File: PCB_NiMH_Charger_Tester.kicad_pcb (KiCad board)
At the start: 2 copper layers, 94.9 x 77.5 mm, 63 parts, among them J1 USB_C_Receptacle_PowerOnly_6P, J2 USB_C_Receptacle_USB2.0_16P, J3 UPDI header, J4 SSD1306, J5 Serial Header, Q1 DTC114EL, Q2 DTA114EL, Q3 MTB060P06I3, Q4 MTA100N10KRI3, SW1 SW_Push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

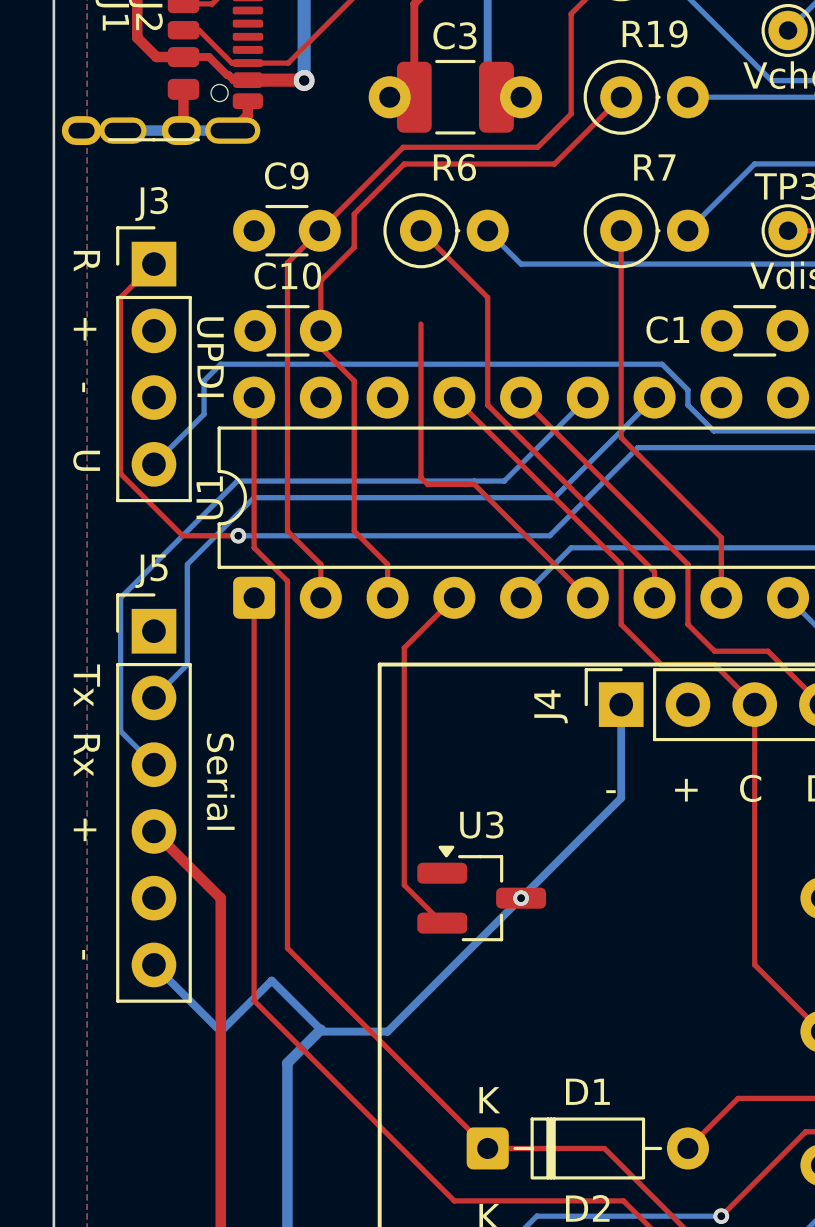
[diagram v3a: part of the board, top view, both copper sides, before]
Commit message: Adjust J3,J5 position
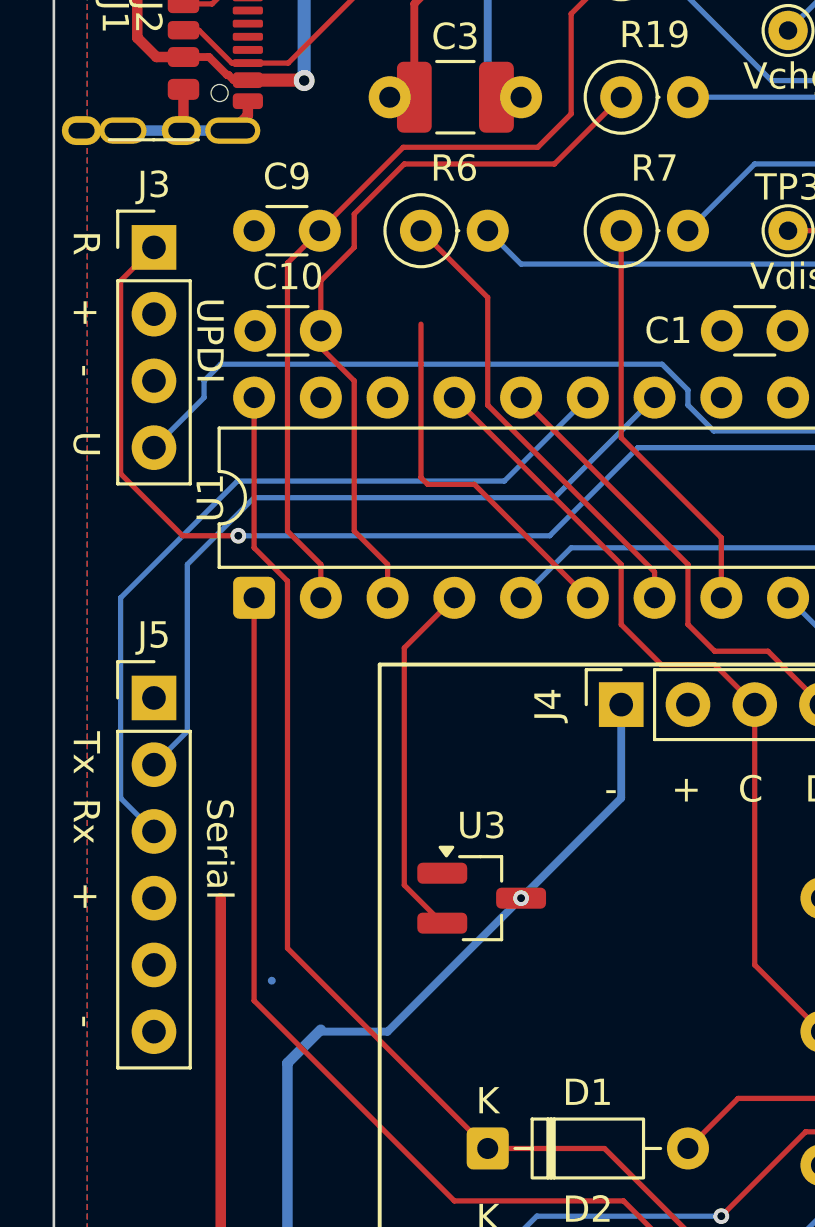
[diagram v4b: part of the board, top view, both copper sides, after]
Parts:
- moved J5 2.54 mm to (53.3, 64.8)
- moved J3 0.63 mm to (53.3, 47.6)
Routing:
- net GND: track 161.9 -> 153.0 mm
- net +5V: track 204.2 -> 200.6 mm
- net TX: track 26.0 -> 28.6 mm
- net RX: track 27.8 -> 30.4 mm
- net UPDI: track 30.9 -> 30.3 mm
- net RESET: track 42.1 -> 42.8 mm
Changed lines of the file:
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@@
 	(footprint "Connector_PinHeader_2.54mm:PinHeader_1x04_P2.54mm_Vertical"
 		(layer "F.Cu")
-		(at 53.34 48.26)
+		(at 53.34 47.625)
 		(descr "Through hole straight pin header, 1x04, 2.54mm pitch, single row")
 		(tags "Through hole pin header THT 1x04 2.54mm single row")
@@
 	(footprint "Connector_PinHeader_2.54mm:PinHeader_1x06_P2.54mm_Vertical"
 		(layer "F.Cu")
-		(at 53.34 62.23)
+		(at 53.34 64.77)
 		(descr "Through hole straight pin header, 1x06, 2.54mm pitch, single row")
 		(tags "Through hole pin header THT 1x06 2.54mm single row")
@@
 	)
 	(gr_text "U"
-		(at 50.165 55.245 270)
+		(at 50.165 54.61 270)
 		(layer "F.SilkS")
 		(effects
@@
 	)
 	(gr_text "UPDI"
-		(at 54.87157 50.165 270)
+		(at 54.87157 49.53 270)
 		(layer "F.SilkS")
 		(effects
@@
 	)
 	(gr_text "Rx"
-		(at 50.165 66.04 270)
+		(at 50.165 68.58 270)
 		(layer "F.SilkS")
 		(effects
@@
 	)
 	(gr_text "Serial"
-		(at 55.245 66.04 270)
+		(at 55.245 68.58 270)
 		(layer "F.SilkS")
 		(effects
@@
 	)
 	(gr_text "R"
-		(at 50.165 47.625 270)
+		(at 50.165 46.99 270)
 		(layer "F.SilkS")
 		(effects
@@
 	)
 	(gr_text "+"
-		(at 50.165 69.215 270)
+		(at 50.165 71.755 270)
 		(layer "F.SilkS")
 		(effects
@@
 	)
 	(gr_text "-"
-		(at 50.165 52.705 270)
+		(at 50.165 52.07 270)
 		(layer "F.SilkS")
 		(effects
@@
 	)
 	(gr_text "Tx"
-		(at 50.165 63.5 270)
+		(at 50.165 66.04 270)
 		(layer "F.SilkS")
 		(effects
@@
 	)
 	(gr_text "-"
-		(at 50.165 74.295 270)
+		(at 50.165 76.835 270)
 		(layer "F.SilkS")
 		(effects
@@
 	)
 	(gr_text "+"
-		(at 50.165 50.165 270)
+		(at 50.165 49.53 270)
 		(layer "F.SilkS")
 		(effects
@@
 	)
 	(segment
-		(start 55.88 77.47)
-		(end 57.82 75.53)
-		(width 0.3)
-		(layer "B.Cu")
-		(net 2)
-	)
-	(segment
 		(start 66.04 35.56)
 		(end 67.31 36.83)
@@
 	)
 	(segment
-		(start 57.825 75.53)
-		(end 59.69 77.395)
-		(width 0.3)
-		(layer "B.Cu")
-		(net 2)
-	)
-	(segment
 		(start 58.42 78.665)
 		(end 59.69 77.395)
@@
 	)
 	(segment
-		(start 53.34 74.93)
-		(end 55.88 77.47)
-		(width 0.3)
-		(layer "B.Cu")
-		(net 2)
-	)
-	(segment
 		(start 116.84 88.9)
 		(end 116.76 88.9)
@@
 	)
 	(segment
-		(start 55.88 72.39)
-		(end 53.34 69.85)
-		(width 0.4)
-		(layer "F.Cu")
-		(net 4)
-	)
-	(segment
 		(start 134.62 96.52)
 		(end 135.89 96.52)
@@
 	)
 	(segment
-		(start 55.245 53.975)
-		(end 53.34 55.88)
+		(start 55.245 53.34)
+		(end 55.245 52.705)
 		(width 0.2)
 		(layer "B.Cu")
@@
 	)
 	(segment
-		(start 78.74 54.61)
-		(end 74.64295 54.61)
+		(start 53.34 55.245)
+		(end 55.245 53.34)
 		(width 0.2)
 		(layer "B.Cu")
@@
 	)
 	(segment
-		(start 55.245 52.705)
-		(end 55.245 53.975)
+		(start 78.74 54.61)
+		(end 74.64295 54.61)
 		(width 0.2)
 		(layer "B.Cu")
@@
 	)
 	(segment
-		(start 54.61 59.69)
-		(end 54.61 63.5)
+		(start 68.58 57.15)
+		(end 72.39 53.34)
 		(width 0.2)
 		(layer "B.Cu")
@@
 	)
 	(segment
-		(start 54.61 63.5)
-		(end 53.34 64.77)
+		(start 53.34 67.31)
+		(end 54.61 66.04)
 		(width 0.2)
 		(layer "B.Cu")
@@
 	)
 	(segment
-		(start 68.58 57.15)
-		(end 57.15 57.15)
+		(start 54.61 66.04)
+		(end 54.61 59.69)
 		(width 0.2)
 		(layer "B.Cu")
@@
 	)
 	(segment
-		(start 57.15 57.15)
-		(end 54.61 59.69)
+		(start 54.61 59.69)
+		(end 57.15 57.15)
 		(width 0.2)
 		(layer "B.Cu")
@@
 	)
 	(segment
-		(start 72.39 53.34)
+		(start 57.15 57.15)
 		(end 68.58 57.15)
 		(width 0.2)
@@
 	)
 	(segment
-		(start 53.34 67.31)
-		(end 52.07 66.04)
-		(width 0.2)
-		(layer "B.Cu")
-		(net 27)
-	)
-	(segment
-		(start 52.07 60.96)
-		(end 56.515 56.515)
+		(start 66.675 56.515)
+		(end 69.85 53.34)
 		(width 0.2)
 		(layer "B.Cu")
@@
 	(segment
 		(start 56.515 56.515)
-		(end 65.532 56.515)
+		(end 66.675 56.515)
 		(width 0.2)
 		(layer "B.Cu")
@@
 	)
 	(segment
-		(start 66.675 56.515)
-		(end 65.532 56.515)
+		(start 53.34 69.85)
+		(end 52.07 68.58)
 		(width 0.2)
 		(layer "B.Cu")
@@
 	)
 	(segment
-		(start 69.85 53.34)
-		(end 66.675 56.515)
+		(start 52.07 68.58)
+		(end 52.07 60.96)
 		(width 0.2)
 		(layer "B.Cu")
@@
 	)
 	(segment
-		(start 52.07 66.04)
-		(end 52.07 60.96)
+		(start 52.07 60.96)
+		(end 56.515 56.515)
 		(width 0.2)
 		(layer "B.Cu")
@@
 	)
 	(segment
-		(start 52.07 49.53)
-		(end 53.34 48.26)
+		(start 53.34 47.625)
+		(end 52.07 48.895)
 		(width 0.2)
 		(layer "F.Cu")
@@
 	)
 	(segment
-		(start 56.55 58.598527)
+		(start 52.07 56.23776)
 		(end 54.430767 58.598527)
 		(width 0.2)
@@
 	)
 	(segment
-		(start 52.07 56.23776)
-		(end 52.07 49.53)
+		(start 52.07 48.895)
+		(end 52.07 56.23776)
 		(width 0.2)
 		(layer "F.Cu")
@@
 	(segment
 		(start 54.430767 58.598527)
-		(end 52.07 56.23776)
+		(end 56.55 58.598527)
 		(width 0.2)
 		(layer "F.Cu")

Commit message: Adjust resistor values
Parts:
- J3: value UPDI header -> UPDI v2 header
- R10, R11: value 1k -> 4.7k
- R12, R15: value 10k -> 47k
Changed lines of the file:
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@@
 			)
 		)
-		(property "Value" "1k"
+		(property "Value" "4.7k"
 			(at 1.27 2.37 0)
 			(layer "F.Fab")
@@
 			)
 		)
-		(property "Value" "10k"
+		(property "Value" "47k"
 			(at 1.27 2.37 0)
 			(layer "F.Fab")
@@
 			)
 		)
-		(property "Value" "UPDI header"
+		(property "Value" "UPDI v2 header"
 			(at 0 10 0)
 			(layer "F.Fab")
@@
 			)
 		)
-		(property "Value" "10k"
+		(property "Value" "47k"
 			(at 1.27 2.37 0)
 			(layer "F.Fab")
@@
 			)
 		)
-		(property "Value" "1k"
+		(property "Value" "4.7k"
 			(at 1.27 2.37 0)
 			(layer "F.Fab")

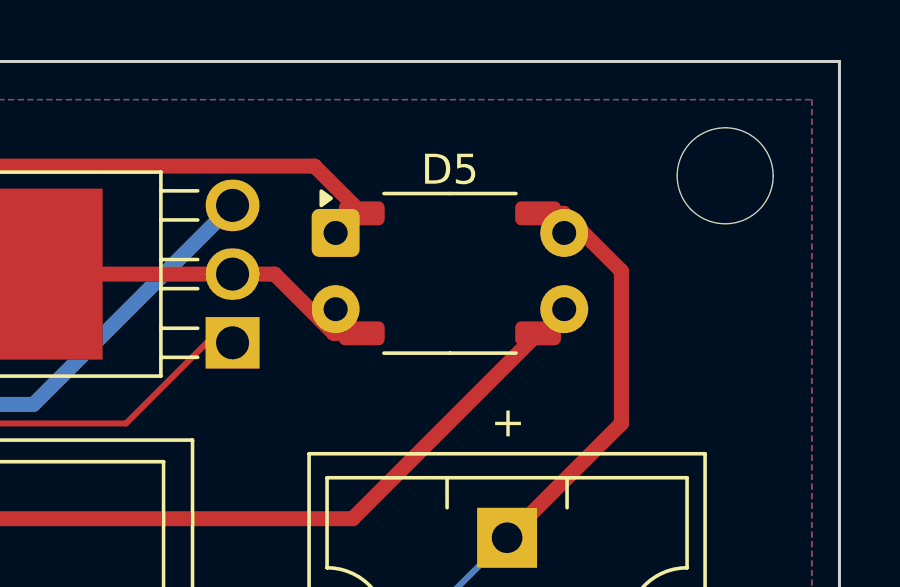
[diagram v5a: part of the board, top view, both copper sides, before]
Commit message: Replace S1ZB20 symbol
It is not a Schottky Bridge, PN Bridge.
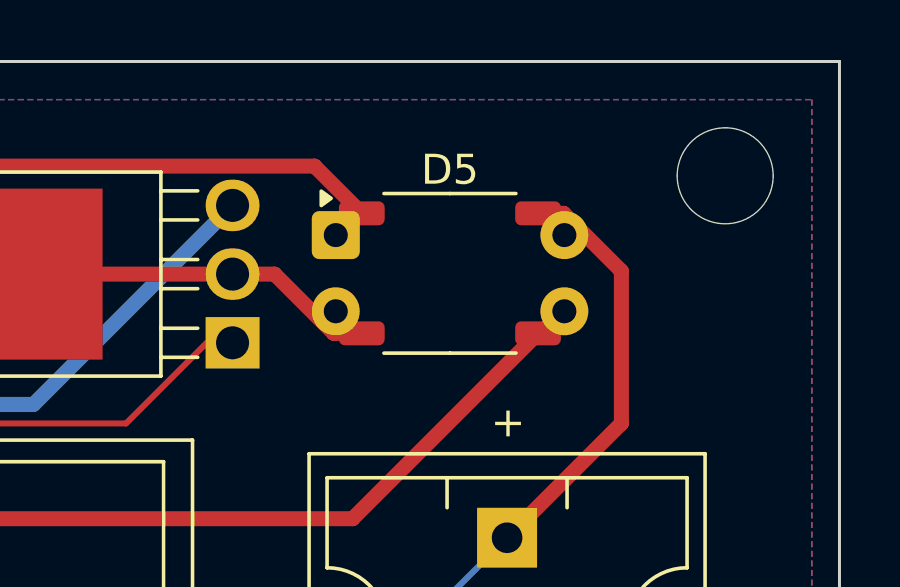
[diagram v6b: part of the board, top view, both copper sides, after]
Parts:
- moved D6 0.07 mm to (127.6, 29.9)
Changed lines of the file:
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@@
 		)
 	)
+	(footprint "Package_DIP:DIP-4_W7.62mm"
+		(layer "F.Cu")
+		(at 127.64 29.9162)
+		(descr "4-lead though-hole mounted DIP package, row spacing 7.62mm (300 mils)")
+		(tags "THT DIP DIL PDIP 2.54mm 7.62mm 300mil")
+		(property "Reference" "D6"
+			(at 3.81 -2.33 0)
+			(layer "F.SilkS")
+			(hide yes)
+			(effects
+				(font
+					(size 1 1)
+					(thickness 0.15)
+				)
+			)
+		)
+		(property "Value" "S1ZB20"
+			(at 3.81 4.87 0)
+			(layer "F.Fab")
+			(effects
+				(font
+					(size 1 1)
+					(thickness 0.15)
+				)
+			)
+		)
+		(property "Datasheet" "https://www.mouser.jp/datasheet/2/366/J534S1ZB-1203344.pdf"
+			(at 0 0 0)
+			(layer "F.Fab")
+			(hide yes)
+			(effects
+				(font
+					(size 1.27 1.27)
+					(thickness 0.15)
+				)
+			)
+		)
+		(property "Description" "Diode Bridge, 200V Vrms, 1A If, DIP-4"
+			(at 0 0 0)
+			(layer "F.Fab")
+			(hide yes)
+			(effects
+				(font
+					(size 1.27 1.27)
+					(thickness 0.15)
+				)
+			)
+		)
+		(property ki_fp_filters "Diode*Bridge*DIP*W7.62mm*P5.08mm*")
+		(sheetname "/")
+		(sheetfile "PCB_NiMH_Charger_Tester.kicad_sch")
+		(attr through_hole dnp)
+		(fp_rect
+			(start -1.06 -1.52)
+			(end 8.67 4.07)
+			(stroke
+				(width 0.05)
+				(type solid)
+			)
+			(fill no)
+			(layer "F.CrtYd")
+		)
+		(fp_line
+			(start 0.635 -0.27)
+			(end 1.635 -1.27)
+			(stroke
+				(width 0.1)
+				(type solid)
+			)
+			(layer "F.Fab")
+		)
+		(fp_line
+			(start 0.635 3.81)
+			(end 0.635 -0.27)
+			(stroke
+				(width 0.1)
+				(type solid)
+			)
+			(layer "F.Fab")
+		)
+		(fp_line
+			(start 1.635 -1.27)
+			(end 6.985 -1.27)
+			(stroke
+				(width 0.1)
+				(type solid)
+			)
+			(layer "F.Fab")
+		)
+		(fp_line
+			(start 6.985 -1.27)
+			(end 6.985 3.81)
+			(stroke
+				(width 0.1)
+				(type solid)
+			)
+			(layer "F.Fab")
+		)
+		(fp_line
+			(start 6.985 3.81)
+			(end 0.635 3.81)
+			(stroke
+				(width 0.1)
+				(type solid)
+			)
+			(layer "F.Fab")
+		)
+		(fp_text user "${REFERENCE}"
+			(at 3.81 1.27 0)
+			(layer "F.Fab")
+			(effects
+				(font
+					(size 1 1)
+					(thickness 0.15)
+				)
+			)
+		)
+		(pad "1" thru_hole roundrect
+			(at 0 0)
+			(size 1.6 1.6)
+			(drill 0.8)
+			(layers "*.Cu" "*.Mask")
+			(remove_unused_layers no)
+			(roundrect_rratio 0.15625)
+			(net 19 "Net-(D5-+)")
+			(pinfunction "+")
+			(pintype "passive")
+		)
+		(pad "2" thru_hole circle
+			(at 0 2.54)
+			(size 1.6 1.6)
+			(drill 0.8)
+			(layers "*.Cu" "*.Mask")
+			(remove_unused_layers no)
+			(net 18 "Net-(D5--)")
+			(pinfunction "-")
+			(pintype "passive")
+		)
+		(pad "3" thru_hole circle
+			(at 7.62 2.54)
+			(size 1.6 1.6)
+			(drill 0.8)
+			(layers "*.Cu" "*.Mask")
+			(remove_unused_layers no)
+			(net 1 "BT1+")
+			(pintype "passive")
+		)
+		(pad "4" thru_hole circle
+			(at 7.62 0)
+			(size 1.6 1.6)
+			(drill 0.8)
+			(layers "*.Cu" "*.Mask")
+			(remove_unused_layers no)
+			(net 3 "BT2+")
+			(pintype "passive")
+		)
+		(embedded_fonts no)
+		(model "${KICAD9_3DMODEL_DIR}/Package_DIP.3dshapes/DIP-4_W7.62mm.step"
+			(offset
+				(xyz 0 0 0)
+			)
+			(scale
+				(xyz 1 1 1)
+			)
+			(rotate
+				(xyz 0 0 0)
+			)
+		)
+	)
 	(footprint "Package_TO_SOT_SMD:SOT-23_Handsoldering"
 		(layer "F.Cu")
@@
 			(offset
 				(xyz 0 0 0)
-			)
-			(scale
-				(xyz 1 1 1)
-			)
-			(rotate
-				(xyz 0 0 0)
-			)
-		)
-	)
-	(footprint "Package_DIP:DIP-4_W7.62mm"
-		(layer "F.Cu")
-		(at 127.635 29.845)
-		(descr "4-lead though-hole mounted DIP package, row spacing 7.62mm (300 mils)")
-		(tags "THT DIP DIL PDIP 2.54mm 7.62mm 300mil")
-		(property "Reference" "D6"
-			(at 3.81 -2.33 0)
-			(layer "F.SilkS")
-			(hide yes)
-			(effects
-				(font
-					(size 1 1)
-					(thickness 0.15)
-				)
-			)
-		)
-		(property "Value" "S1ZB20"
-			(at 3.81 6.35 0)
-			(layer "F.Fab")
-			(effects
-				(font
-					(size 1 1)
-					(thickness 0.15)
-				)
-			)
-		)
-		(property "Datasheet" "https://www.mouser.jp/datasheet/2/366/J534S1ZB-1203344.pdf"
-			(at 0 0 0)
-			(layer "F.Fab")
-			(hide yes)
-			(effects
-				(font
-					(size 1.27 1.27)
-					(thickness 0.15)
-				)
-			)
-		)
-		(property "Description" "Schottky Bridge, 200V Vrms, 1A If, DIP-4"
-			(at 0 0 0)
-			(layer "F.Fab")
-			(hide yes)
-			(effects
-				(font
-					(size 1.27 1.27)
-					(thickness 0.15)
-				)
-			)
-		)
-		(property ki_fp_filters "TSSOP*4.4x5mm*P4mm*")
-		(sheetname "/")
-		(sheetfile "PCB_NiMH_Charger_Tester.kicad_sch")
-		(attr through_hole dnp)
-		(fp_rect
-			(start -1.06 -1.52)
-			(end 8.67 4.07)
-			(stroke
-				(width 0.05)
-				(type solid)
-			)
-			(fill no)
-			(layer "F.CrtYd")
-		)
-		(fp_line
-			(start 0.635 -0.27)
-			(end 1.635 -1.27)
-			(stroke
-				(width 0.1)
-				(type solid)
-			)
-			(layer "F.Fab")
-		)
-		(fp_line
-			(start 0.635 3.81)
-			(end 0.635 -0.27)
-			(stroke
-				(width 0.1)
-				(type solid)
-			)
-			(layer "F.Fab")
-		)
-		(fp_line
-			(start 1.635 -1.27)
-			(end 6.985 -1.27)
-			(stroke
-				(width 0.1)
-				(type solid)
-			)
-			(layer "F.Fab")
-		)
-		(fp_line
-			(start 6.985 -1.27)
-			(end 6.985 3.81)
-			(stroke
-				(width 0.1)
-				(type solid)
-			)
-			(layer "F.Fab")
-		)
-		(fp_line
-			(start 6.985 3.81)
-			(end 0.635 3.81)
-			(stroke
-				(width 0.1)
-				(type solid)
-			)
-			(layer "F.Fab")
-		)
-		(fp_text user "${REFERENCE}"
-			(at 3.81 1.27 0)
-			(layer "F.Fab")
-			(effects
-				(font
-					(size 1 1)
-					(thickness 0.15)
-				)
-			)
-		)
-		(pad "1" thru_hole roundrect
-			(at 0 0)
-			(size 1.6 1.6)
-			(drill 0.8)
-			(layers "*.Cu" "*.Mask")
-			(remove_unused_layers no)
-			(roundrect_rratio 0.15625)
-			(net 19 "Net-(D5-+)")
-			(pinfunction "+")
-			(pintype "passive")
-		)
-		(pad "2" thru_hole circle
-			(at 0 2.54)
-			(size 1.6 1.6)
-			(drill 0.8)
-			(layers "*.Cu" "*.Mask")
-			(remove_unused_layers no)
-			(net 18 "Net-(D5--)")
-			(pinfunction "-")
-			(pintype "passive")
-		)
-		(pad "3" thru_hole circle
-			(at 7.62 2.54)
-			(size 1.6 1.6)
-			(drill 0.8)
-			(layers "*.Cu" "*.Mask")
-			(remove_unused_layers no)
-			(net 1 "BT1+")
-			(pintype "passive")
-		)
-		(pad "4" thru_hole circle
-			(at 7.62 0)
-			(size 1.6 1.6)
-			(drill 0.8)
-			(layers "*.Cu" "*.Mask")
-			(remove_unused_layers no)
-			(net 3 "BT2+")
-			(pintype "passive")
-		)
-		(embedded_fonts no)
-		(model "${KICAD9_3DMODEL_DIR}/Package_DIP.3dshapes/DIP-4_W7.62mm.step"
-			(offset
-				(xyz 0 0 0)
